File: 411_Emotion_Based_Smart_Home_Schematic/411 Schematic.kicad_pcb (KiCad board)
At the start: 2 copper layers, 7 parts, among them J1 Barrel_Jack, Q1 IRLB8721PBF, U1 LD1117S33TR_SOT223

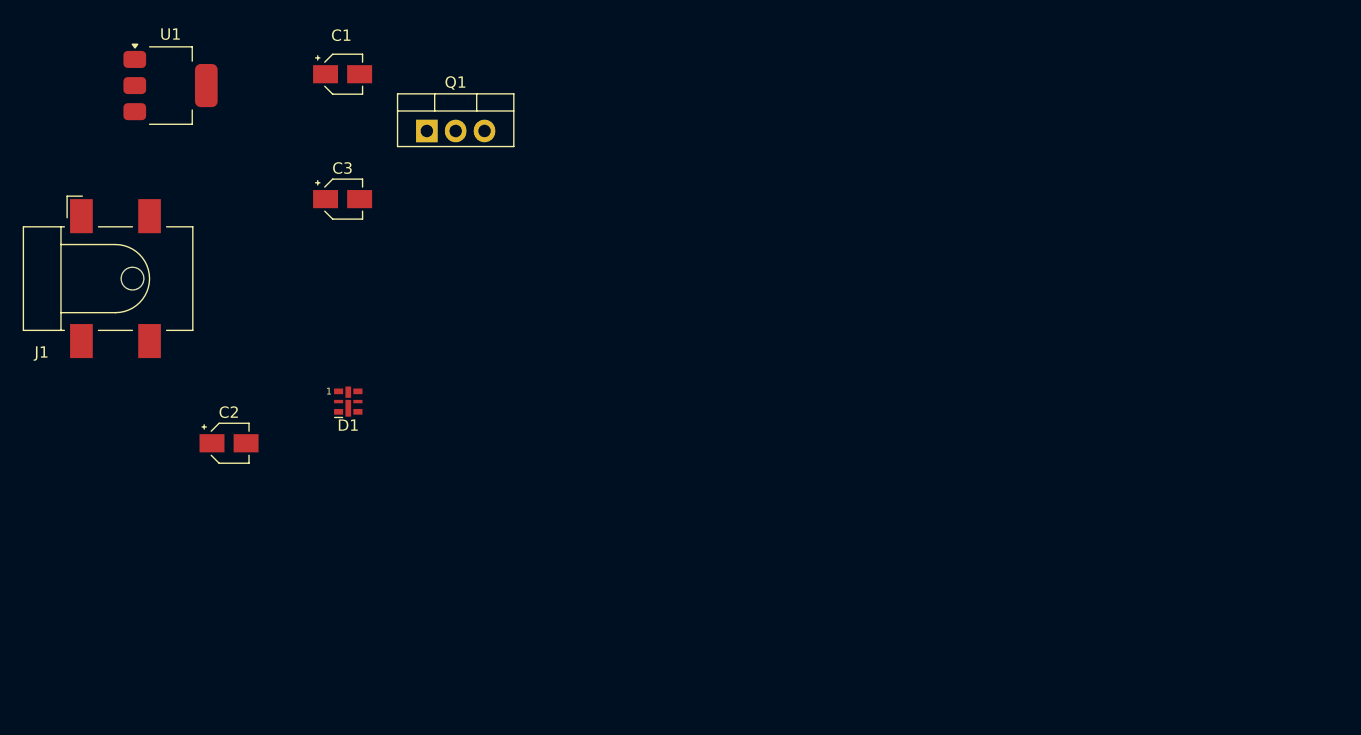
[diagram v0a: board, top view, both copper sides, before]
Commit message: Updating our Schematic and Layout
Altering things in the schematic and layout before we turn this in
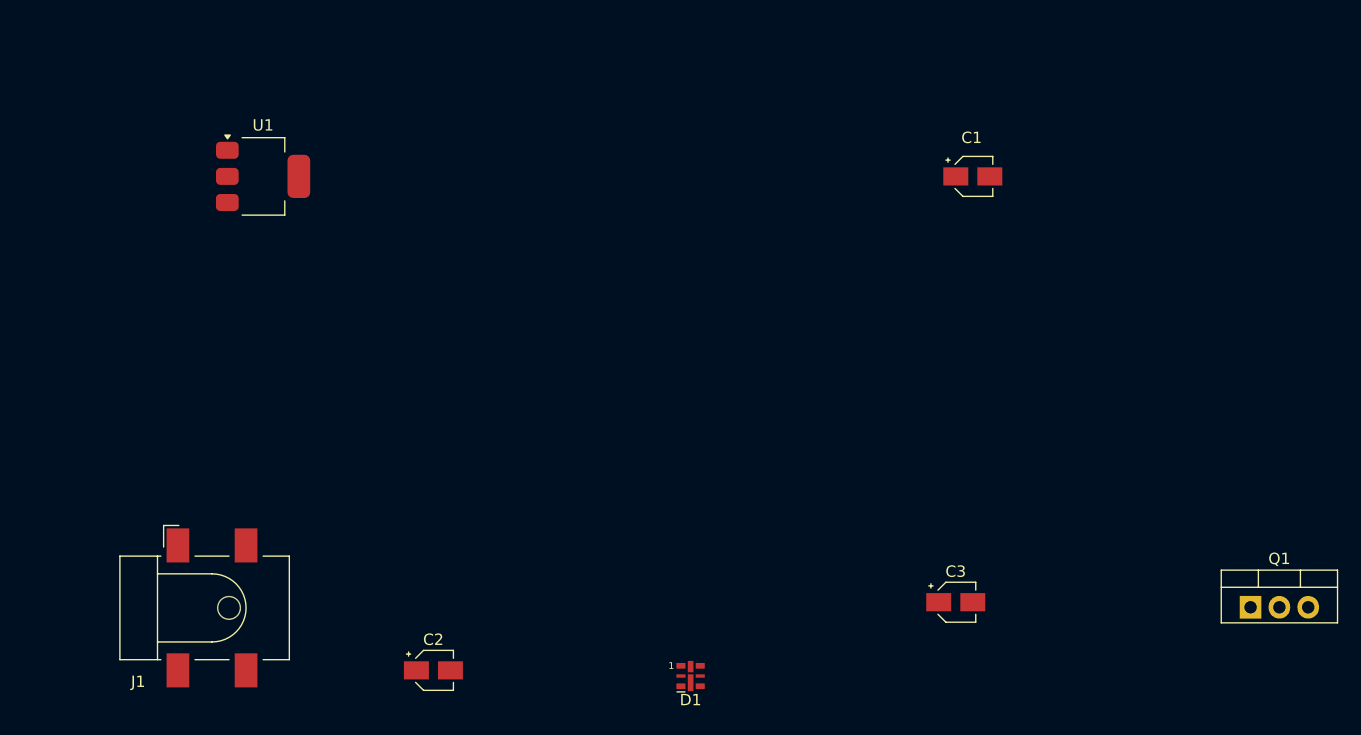
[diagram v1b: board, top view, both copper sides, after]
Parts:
- moved Q1 83.8 mm to (213.5, 112.4)
- moved C3 64.6 mm to (187.5, 112.0)
- moved C1 56.2 mm to (189.0, 74.5)
- moved D1 38.6 mm to (164.2, 118.5)
- moved J1 30.2 mm to (122.0, 112.5)
- moved C2 26.9 mm to (141.5, 118.0)
- moved U1 11.4 mm to (126.5, 74.5)
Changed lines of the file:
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@@
 	)
 	(paper "A4")
+	(title_block
+		(title "Preliminary PCB layout")
+		(date "2024-11-06")
+		(rev "0")
+		(company "Group 6")
+	)
 	(layers
 		(0 "F.Cu" signal)
@@
 	(footprint "Capacitor_SMD:CP_Elec_3x5.3"
 		(layer "F.Cu")
-		(at 123.5 98)
+		(at 141.5 118)
 		(descr "SMT capacitor, aluminium electrolytic, 3x5.3, Cornell Dubilier Electronics ")
 		(tags "Capacitor Electrolytic")
@@
 	(footprint "LED_SMD:LED-APA102-2020"
 		(layer "F.Cu")
-		(at 134 94.33)
+		(at 164.15 118.5)
 		(descr "http://www.led-color.com/upload/201604/APA102-2020%20SMD%20LED.pdf")
 		(tags "LED RGB SPI")
@@
 	(footprint "Package_TO_SOT_THT:TO-220-3_Vertical"
 		(layer "F.Cu")
-		(at 140.92 70.5)
+		(at 213.46 112.445)
 		(descr "TO-220-3, Vertical, RM 2.54mm, see https://www.vishay.com/docs/66542/to-220-1.pdf")
 		(tags "TO-220-3 Vertical RM 2.54mm")
@@
 	(footprint "Package_TO_SOT_SMD:SOT-223-3_TabPin2"
 		(layer "F.Cu")
-		(at 118.35 66.5)
+		(at 126.5 74.5)
 		(descr "module CMS SOT223 4 pins")
 		(tags "CMS SOT")
@@
 		)
 		(property "Value" "LD1117S33TR_SOT223"
-			(at -4.5 -11 0)
+			(at 0 -18.5 0)
 			(layer "F.Fab")
 			(effects
@@
 	(footprint "Capacitor_SMD:CP_Elec_3x5.3"
 		(layer "F.Cu")
-		(at 133.5 65.5)
+		(at 189 74.5)
 		(descr "SMT capacitor, aluminium electrolytic, 3x5.3, Cornell Dubilier Electronics ")
 		(tags "Capacitor Electrolytic")
@@
 	(footprint "Connector_BarrelJack:BarrelJack_CLIFF_FC681465S_SMT_Horizontal"
 		(layer "F.Cu")
-		(at 113.5 83.5)
+		(at 122 112.5)
 		(descr "Surface-mount DC Barrel Jack, https://www.cliffuk.co.uk/products/dcconnectors/FC681465S.pdf")
 		(tags "Power Jack SMT")
@@
 	(footprint "Capacitor_SMD:CP_Elec_3x5.3"
 		(layer "F.Cu")
-		(at 133.5 76.5)
+		(at 187.5 112)
 		(descr "SMT capacitor, aluminium electrolytic, 3x5.3, Cornell Dubilier Electronics ")
 		(tags "Capacitor Electrolytic")

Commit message: PCB Rough route and schematic almost finished
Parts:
- removed C1, C3: 10uF, Capacitor_SMD:CP_Elec_3x5.3
- removed C2: 10uf, Capacitor_SMD:CP_Elec_3x5.3
- removed J1: Barrel_Jack, Connector_BarrelJack:BarrelJack_CLIFF_FC681465S_SMT_Horizontal
- removed U1: LD1117S33TR_SOT223, Package_TO_SOT_SMD:SOT-223-3_TabPin2
- added D2: Inolux_IN-P55TATRGB, LED_SMD:LED_Inolux_IN-P55TATRGB_PLCC6_5.0x5.5mm_P1.8mm, F.Cu at (136.9, 91.1)
- added D3: Inolux_IN-P55TATRGB, LED_SMD:LED_Inolux_IN-P55TATRGB_PLCC6_5.0x5.5mm_P1.8mm, F.Cu at (164.3, 90.9)
- added Jetson_40-Pin1: ~, Connector_PinHeader_2.54mm:PinHeader_2x40_P2.54mm_Vertical, F.Cu at (184.0, 115.0)
- added Q2: NSS1C301ET4G, Transistor411Library:DPAK-4_6P22X6P73_ONS, F.Cu at (121.8, 100.1)
- added Q3: NSS1C301ET4G, Transistor411Library:DPAK-4_6P22X6P73_ONS, F.Cu at (150.3, 99.4)
- added U4: HC-SR04, Connector_PinSocket_2.54mm:PinSocket_1x04_P2.54mm_Vertical, F.Cu at (182.3, 90.4)
- D1: value LED -> Inolux_IN-P55TATRGB; footprint LED_SMD:LED-APA102-2020 -> LED_SMD:LED_Inolux_IN-P55TATRGB_PLCC6_5.0x5.5mm_P1.8mm
- Q1: value IRLB8721PBF -> NSS1C301ET4G; footprint Package_TO_SOT_THT:TO-220-3_Vertical -> Transistor411Library:DPAK-4_6P22X6P73_ONS
- moved Q1 120.3 mm to (93.8, 100.6)
- moved D1 63.2 mm to (107.3, 91.0), turned to -90 degrees
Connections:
- D1 pad 2: Net-(D1-A) -> GND
- D1 pad 3: (no net) -> GND
- D1 pad 4: (no net) -> Q1
- D1 pad 5: (no net) -> Q3
- D1 pad 6: (no net) -> Q2
- Q1 pad 1: /LED_ON 3.3V -> Net-(Jetson_40-Pin1-GPIO13)
- Q1 pad 2: /4V -> Net-(Q1-C)
- Q1 pad 3: +9V -> Q1
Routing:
- net GND: track 0.00 -> 264.2 mm
- net Q2: track 0.00 -> 207.4 mm
- net Q1: track 0.00 -> 132.9 mm
- net Net-(Jetson_40-Pin1-GPIO01): track 0.00 -> 129.8 mm
- net Net-(Q1-C): track 0.00 -> 94.1 mm
- net Q3: track 0.00 -> 90.5 mm
- net Net-(Jetson_40-Pin1-GPIO11): track 0.00 -> 81.9 mm
- net /5V: track 0.00 -> 79.0 mm
- net Net-(Jetson_40-Pin1-GPIO13): track 0.00 -> 55.2 mm
- net /Ultrasonic Trigger: track 0.00 -> 47.4 mm
- net Net-(Jetson_40-Pin1-UART1_RXD): track 0.00 -> 37.2 mm
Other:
- board outline added: 110 x 40 mm

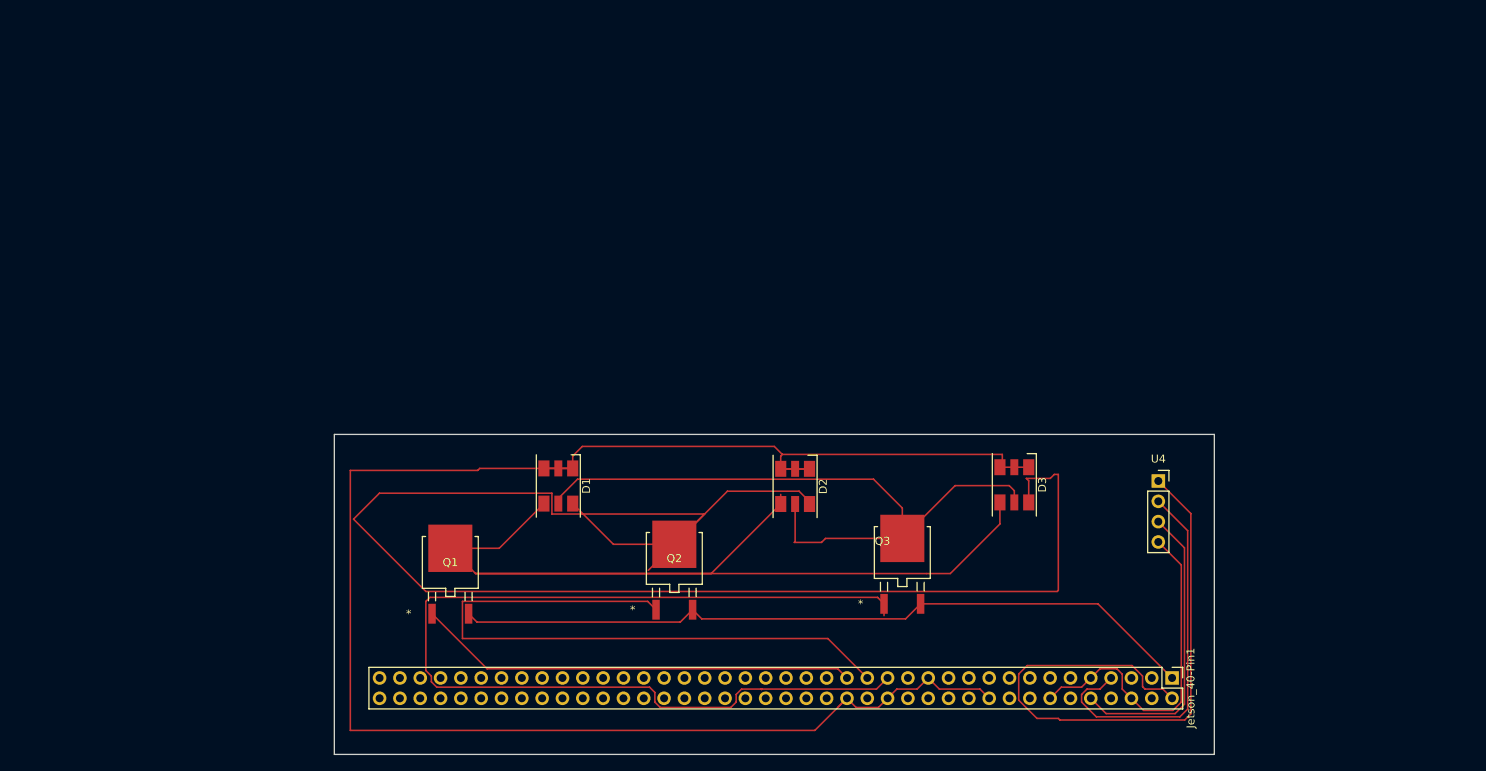
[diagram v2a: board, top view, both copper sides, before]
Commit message: Modified size of PCB frame
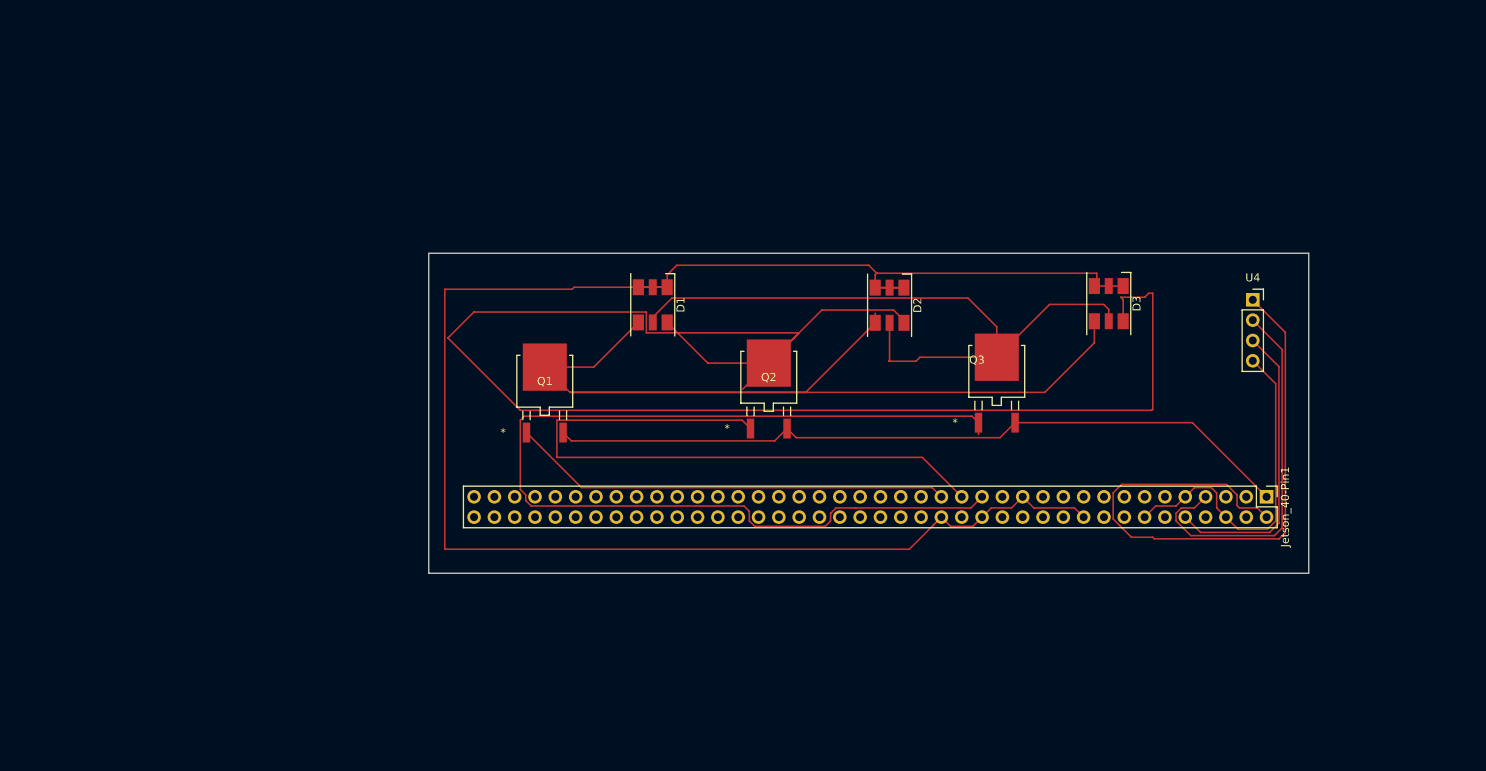
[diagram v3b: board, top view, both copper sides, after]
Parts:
- moved U4 25.5 mm to (194.1, 67.8)
- moved D1 25.5 mm to (119.1, 68.4)
- moved D2 25.5 mm to (148.7, 68.4)
- moved D3 25.5 mm to (176.1, 68.2)
- moved Jetson_40-Pin1 25.5 mm to (195.8, 92.4)
- moved Q1 25.5 mm to (105.6, 77.9)
- moved Q3 25.5 mm to (162.1, 76.7)
- moved Q2 25.5 mm to (133.6, 77.4)

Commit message: Removing .lck files agian
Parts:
- moved D1 47.5 mm to (82.0, 38.8)
- moved D2 47.5 mm to (111.6, 38.8)
- moved Jetson_40-Pin1 47.5 mm to (158.7, 62.8)
- moved Q1 47.5 mm to (68.5, 48.3)
- moved D3 47.5 mm to (139.0, 38.6)
- moved Q2 47.5 mm to (96.5, 47.8)
- moved Q3 47.5 mm to (125.0, 47.1)
- moved U4 47.5 mm to (157.0, 38.1)

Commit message: Updated schematic.
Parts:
- removed D3: Inolux_IN-P55TATRGB, LED_SMD:LED_Inolux_IN-P55TATRGB_PLCC6_5.0x5.5mm_P1.8mm
- added D4: LED_RGB, LED_SMD:LED_RGB_5050-6, F.Cu at (62.7, 80.6)
- added R1: 10, Resistor_THT:R_Axial_DIN0411_L9.9mm_D3.6mm_P5.08mm_Vertical, F.Cu at (86.6, 64.1)
- added R2: 10, Resistor_THT:R_Axial_DIN0411_L9.9mm_D3.6mm_P5.08mm_Vertical, F.Cu at (86.5, 80.1)
- added R3: 10, Resistor_THT:R_Axial_DIN0411_L9.9mm_D3.6mm_P5.08mm_Vertical, F.Cu at (86.5, 72.1)
- D1, D2: value Inolux_IN-P55TATRGB -> LED_RGB; footprint LED_SMD:LED_Inolux_IN-P55TATRGB_PLCC6_5.0x5.5mm_P1.8mm -> LED_SMD:LED_RGB_5050-6
- Q1, Q2, Q3: footprint Transistor411Library:DPAK-4_6P22X6P73_ONS -> NSS1C301ET4G:DPAK-4_6P22X6P73_ONS
- moved D2 52.9 mm to (62.7, 59.1), turned to 0 degrees
- moved U4 48.2 mm to (148.0, 85.5), turned to -90 degrees
- moved Q1 39.6 mm to (104.0, 65.8)
- moved D1 33.2 mm to (74.7, 71.1), turned to 0 degrees
- moved Jetson_40-Pin1 32.5 mm to (148.1, 93.5)
- moved Q2 27.6 mm to (117.5, 65.8)
- moved Q3 19.5 mm to (130.5, 65.8)
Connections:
- D1 pad 4: Q1 -> Q2
- D1 pad 5: Q3 -> Q1
- D1 pad 6: Q2 -> Q3
- D2 pad 4: Q1 -> Q2
- D2 pad 5: Q3 -> Q1
- D2 pad 6: Q2 -> Q3
- Jetson_40-Pin1 pad 1: Net-(Q1-C) -> unconnected-(Jetson_40-Pin1-3.3V-Pad1)
- Jetson_40-Pin1 pad 10: Net-(Jetson_40-Pin1-UART1_RXD) -> unconnected-(Jetson_40-Pin1-UART1_RXD-Pad10)
- Jetson_40-Pin1 pad 14: GND -> unconnected-(Jetson_40-Pin1-GND-Pad14)
- Jetson_40-Pin1 pad 15: unconnected-(Jetson_40-Pin1-GPIO12-Pad15) -> Net-(Jetson_40-Pin1-GPIO12)
- Jetson_40-Pin1 pad 20: GND -> unconnected-(Jetson_40-Pin1-GND-Pad20)
- Jetson_40-Pin1 pad 25: GND -> unconnected-(Jetson_40-Pin1-GND-Pad25)
- Jetson_40-Pin1 pad 30: GND -> unconnected-(Jetson_40-Pin1-GND-Pad30)
- Jetson_40-Pin1 pad 34: GND -> unconnected-(Jetson_40-Pin1-GND-Pad34)
- Jetson_40-Pin1 pad 6: GND -> unconnected-(Jetson_40-Pin1-GND-Pad6)
- Jetson_40-Pin1 pad 9: GND -> Net-(U4-GND)
- Q1 pad 2: Net-(Q1-C) -> /5V
- Q1 pad 3: Q1 -> Net-(Q1-E)
- Q2 pad 2: Net-(Q1-C) -> /5V
- Q2 pad 3: Q2 -> Net-(Q2-E)
- Q3 pad 2: Net-(Q1-C) -> /5V
- Q3 pad 3: Q3 -> Net-(Q3-E)
- U4 pad 3: Net-(Jetson_40-Pin1-UART1_RXD) -> Net-(Jetson_40-Pin1-GPIO12)
- U4 pad 4: GND -> Net-(U4-GND)
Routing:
- net GND: track 264.2 -> 88.9 mm
- net Q2: track 207.4 -> 47.6 mm, vias 0 -> 2
- net Net-(Jetson_40-Pin1-GPIO01): track 129.8 -> 29.8 mm, vias 0 -> 1
- net Net-(Q1-C): track 94.1 -> 0.00 mm
- net Q1: track 132.9 -> 47.9 mm
- net Net-(Jetson_40-Pin1-GPIO11): track 81.9 -> 25.1 mm, vias 0 -> 1
- net Net-(Q3-E): track 0.00 -> 47.6 mm
- net Net-(Q2-E): track 0.00 -> 46.7 mm, vias 0 -> 1
- net /Ultrasonic Trigger: track 47.4 -> 10.0 mm
- net Net-(Jetson_40-Pin1-UART1_RXD): track 37.2 -> 0.00 mm
- net Net-(Jetson_40-Pin1-GPIO13): track 55.2 -> 23.7 mm, vias 0 -> 1
- net Q3: track 90.5 -> 59.9 mm, vias 0 -> 2
- net Net-(Jetson_40-Pin1-GPIO12): track 0.00 -> 22.3 mm
- net Net-(Q1-E): track 0.00 -> 15.8 mm
- net /5V: track 79.0 -> 69.5 mm
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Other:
- board size 110 x 40 mm -> 110 x 46 mm
- board text added: "Team 6 Emotion-Based-Smart-Home-System"

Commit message: Updated schematic.
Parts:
- added R4: 10k, Resistor_THT:R_Axial_DIN0411_L9.9mm_D3.6mm_P5.08mm_Vertical, F.Cu at (116.5, 84.2)
- added R5: 10k, Resistor_THT:R_Axial_DIN0411_L9.9mm_D3.6mm_P5.08mm_Vertical, F.Cu at (128.5, 84.2)
- added R6: 10k, Resistor_THT:R_Axial_DIN0411_L9.9mm_D3.6mm_P5.08mm_Vertical, F.Cu at (106.0, 84.2)
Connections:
- Jetson_40-Pin1 pad 1: unconnected-(Jetson_40-Pin1-3.3V-Pad1) -> Net-(Jetson_40-Pin1-3.3V)
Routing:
- net Net-(Jetson_40-Pin1-3.3V): track 0.00 -> 48.9 mm
- net Net-(Jetson_40-Pin1-GPIO13): track 23.7 -> 32.4 mm
- net Net-(Jetson_40-Pin1-GPIO11): track 25.1 -> 32.6 mm
- net Net-(Jetson_40-Pin1-GPIO01): track 29.8 -> 36.9 mm
